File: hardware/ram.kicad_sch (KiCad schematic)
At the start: 17 parts, among them U10 IS42S16320D-6BLI, U4 CCGM1A1

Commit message: Cleanup
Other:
- moved on the sheet: C57, C58, C75, C76, C77, C78, C79, C80, R119, R120, U4F

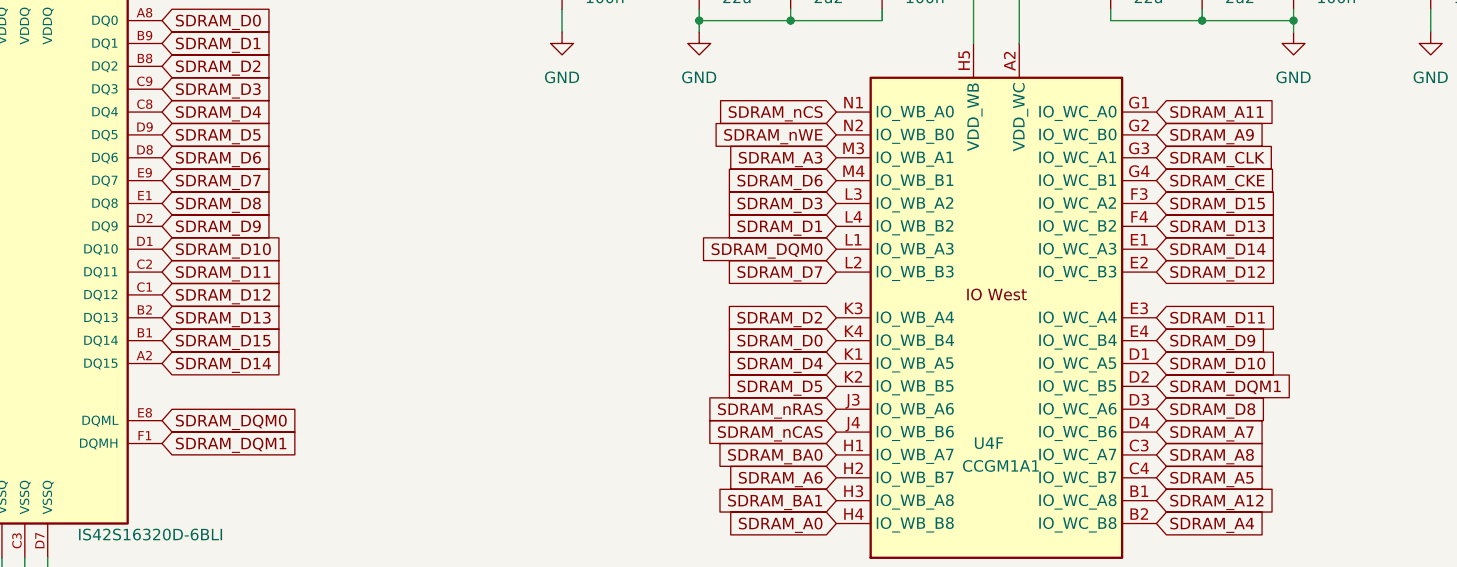
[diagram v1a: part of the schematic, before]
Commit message: fix #1 by renaming - no real change was done
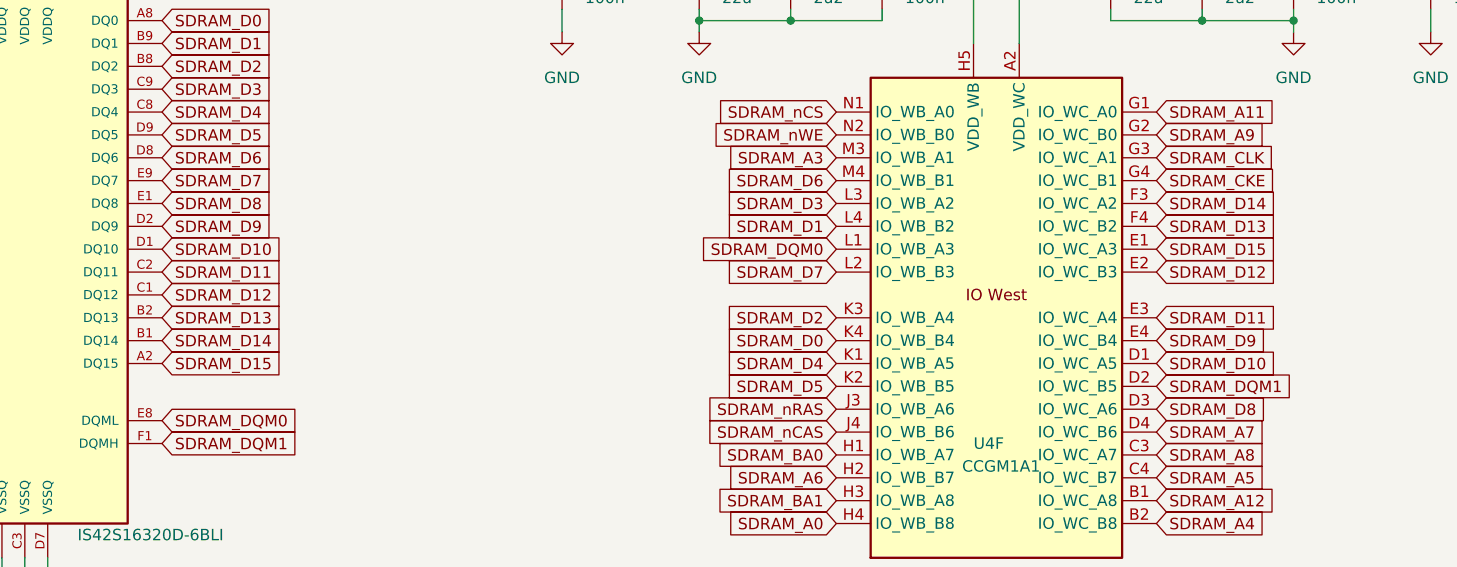
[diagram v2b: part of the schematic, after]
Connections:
- net SDRAM_D14: now also U10.B1 (DQ14), U4.F3 (IO_WC_A2); no longer U10.A2 (DQ15), U4.E1 (IO_WC_A3)
- net SDRAM_D15: now also U10.A2 (DQ15), U4.E1 (IO_WC_A3); no longer U10.B1 (DQ14), U4.F3 (IO_WC_A2)

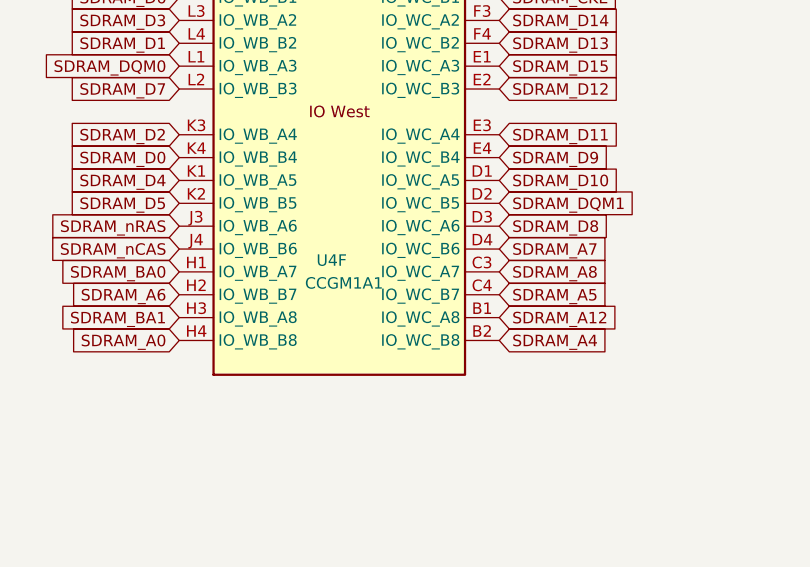
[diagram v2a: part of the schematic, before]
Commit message: Connecting PWR and FAN_PWM to NC pins, using NC3 for Ethernet clock
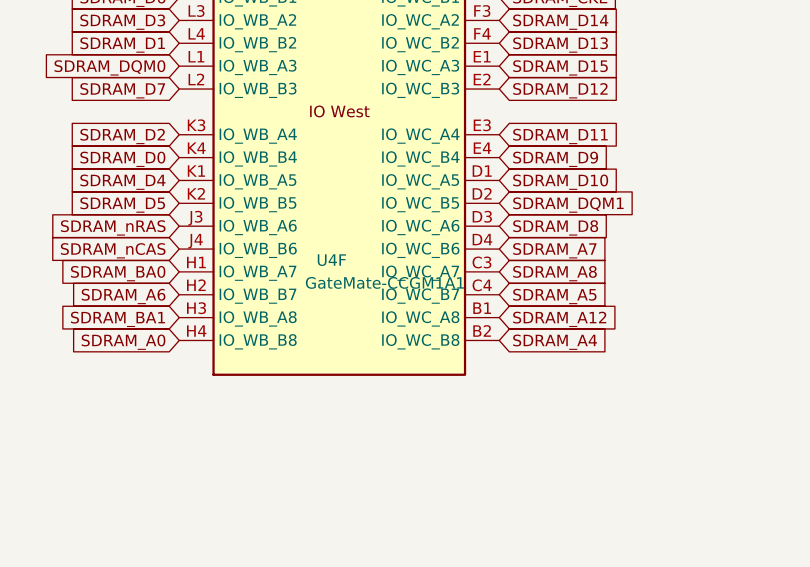
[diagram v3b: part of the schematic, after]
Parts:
- C141, C85: footprint Capacitor_SMD:C_0603_1608Metric -> Capacitor_SMD:C_0402_1005Metric
- U4: value CCGM1A1 -> GateMate-CCGM1A1
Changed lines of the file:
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@@
 			)
 		)
-		(property "Footprint" "Capacitor_SMD:C_0603_1608Metric"
+		(property "Footprint" "Capacitor_SMD:C_0402_1005Metric"
 			(at 70.8152 134.62 0)
 			(effects
@@
 			)
 		)
-		(property "Value" "CCGM1A1"
+		(property "Value" "GateMate-CCGM1A1"
 			(at 193.04 88.9 0)
 			(effects
@@
 			)
 		)
-		(property "Footprint" "Capacitor_SMD:C_0603_1608Metric"
+		(property "Footprint" "Capacitor_SMD:C_0402_1005Metric"
 			(at 102.5652 134.62 0)
 			(effects

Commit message: CleanUP
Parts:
- removed R119, R120: 4R7, Resistor_SMD:R_0402_1005Metric, symbol Device:R_Small
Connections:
- net VCC_WB is gone; now on net SDRAM_VCC: C58.1, C75.1, C76.1, U4.H5 (VDD_WB), U4.J2 (VDD_WB), U4.K5 (VDD_WB), U4.M2 (VDD_WB), U4.M5 (VDD_WB)
- net VCC_WC is gone; now on net SDRAM_VCC: C77.1, C78.1, C79.1, U4.A2 (VDD_WC), U4.C2 (VDD_WC), U4.D5 (VDD_WC), U4.F2 (VDD_WC), U4.F5 (VDD_WC)
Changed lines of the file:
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@@
-	(wire
-		(pts
-			(xy 160.02 31.75) (xy 163.83 31.75)
-		)
-		(stroke
-			(width 0)
-			(type default)
-		)
-	)
 	(wire
 		(pts
@@
 	(wire
 		(pts
-			(xy 241.3 31.75) (xy 245.11 31.75)
-		)
-		(stroke
-			(width 0)
-			(type default)
-		)
-	)
-	(wire
-		(pts
 			(xy 184.15 39.37) (xy 184.15 38.1)
 		)
@@
 	(wire
 		(pts
-			(xy 148.59 31.75) (xy 154.94 31.75)
+			(xy 148.59 31.75) (xy 163.83 31.75)
 		)
 		(stroke
@@
 	(wire
 		(pts
-			(xy 229.87 31.75) (xy 236.22 31.75)
+			(xy 229.87 31.75) (xy 245.11 31.75)
 		)
 		(stroke
@@
 	)
 	(symbol
-		(lib_id "Device:R_Small")
-		(at 238.76 31.75 90)
-		(unit 1)
-		(exclude_from_sim no)
-		(in_bom yes)
-		(on_board yes)
-		(dnp no)
-		(property "Reference" "R119"
-			(at 238.76 26.67 90)
-			(effects
-				(font
-					(size 1.27 1.27)
-				)
-			)
-		)
-		(property "Value" "4R7"
-			(at 238.76 29.21 90)
-			(effects
-				(font
-					(size 1.27 1.27)
-				)
-			)
-		)
-		(property "Footprint" "Resistor_SMD:R_0402_1005Metric"
-			(at 238.76 31.75 0)
-			(effects
-				(font
-					(size 1.27 1.27)
-				)
-				(hide yes)
-			)
-		)
-		(property "Datasheet" "~"
-			(at 238.76 31.75 0)
-			(effects
-				(font
-					(size 1.27 1.27)
-				)
-				(hide yes)
-			)
-		)
-		(property "Description" "Resistor, small symbol"
-			(at 238.76 31.75 0)
-			(effects
-				(font
-					(size 1.27 1.27)
-				)
-				(hide yes)
-			)
-		)
-		(pin "1"
-		)
-		(pin "2"
-		)
-		(instances
-			(project "gatemate-plm"
-				(path "/9e5cbfd6-8186-4817-919e-acd256336bc8/e7f41e58-8517-469c-9a21-6f6a704f2114"
-					(reference "R119")
-					(unit 1)
-				)
-			)
-		)
-	)
-	(symbol
 		(lib_id "power:VCC")
 		(at 78.74 127 0)
@@
 					(unit 1)
 				)
-			)
-		)
-	)
-	(symbol
-		(lib_id "Device:R_Small")
-		(at 157.48 31.75 90)
-		(unit 1)
-		(exclude_from_sim no)
-		(in_bom yes)
-		(on_board yes)
-		(dnp no)
-		(property "Reference" "R120"
-			(at 157.48 26.67 90)
-			(effects
-				(font
-					(size 1.27 1.27)
-				)
-			)
-		)
-		(property "Value" "4R7"
-			(at 157.48 29.21 90)
-			(effects
-				(font
-					(size 1.27 1.27)
-				)
-			)
-		)
-		(property "Footprint" "Resistor_SMD:R_0402_1005Metric"
-			(at 157.48 31.75 0)
-			(effects
-				(font
-					(size 1.27 1.27)
-				)
-				(hide yes)
-			)
-		)
-		(property "Datasheet" "~"
-			(at 157.48 31.75 0)
-			(effects
-				(font
-					(size 1.27 1.27)
-				)
-				(hide yes)
-			)
-		)
-		(property "Description" "Resistor, small symbol"
-			(at 157.48 31.75 0)
-			(effects
-				(font
-					(size 1.27 1.27)
-				)
-				(hide yes)
-			)
-		)
-		(pin "1"
-		)
-		(pin "2"
-		)
-		(instances
-			(project "gatemate-plm"
-				(path "/9e5cbfd6-8186-4817-919e-acd256336bc8/e7f41e58-8517-469c-9a21-6f6a704f2114"
-					(reference "R120")
-					(unit 1)
-				)
